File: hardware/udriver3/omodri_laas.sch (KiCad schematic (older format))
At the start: 0 parts

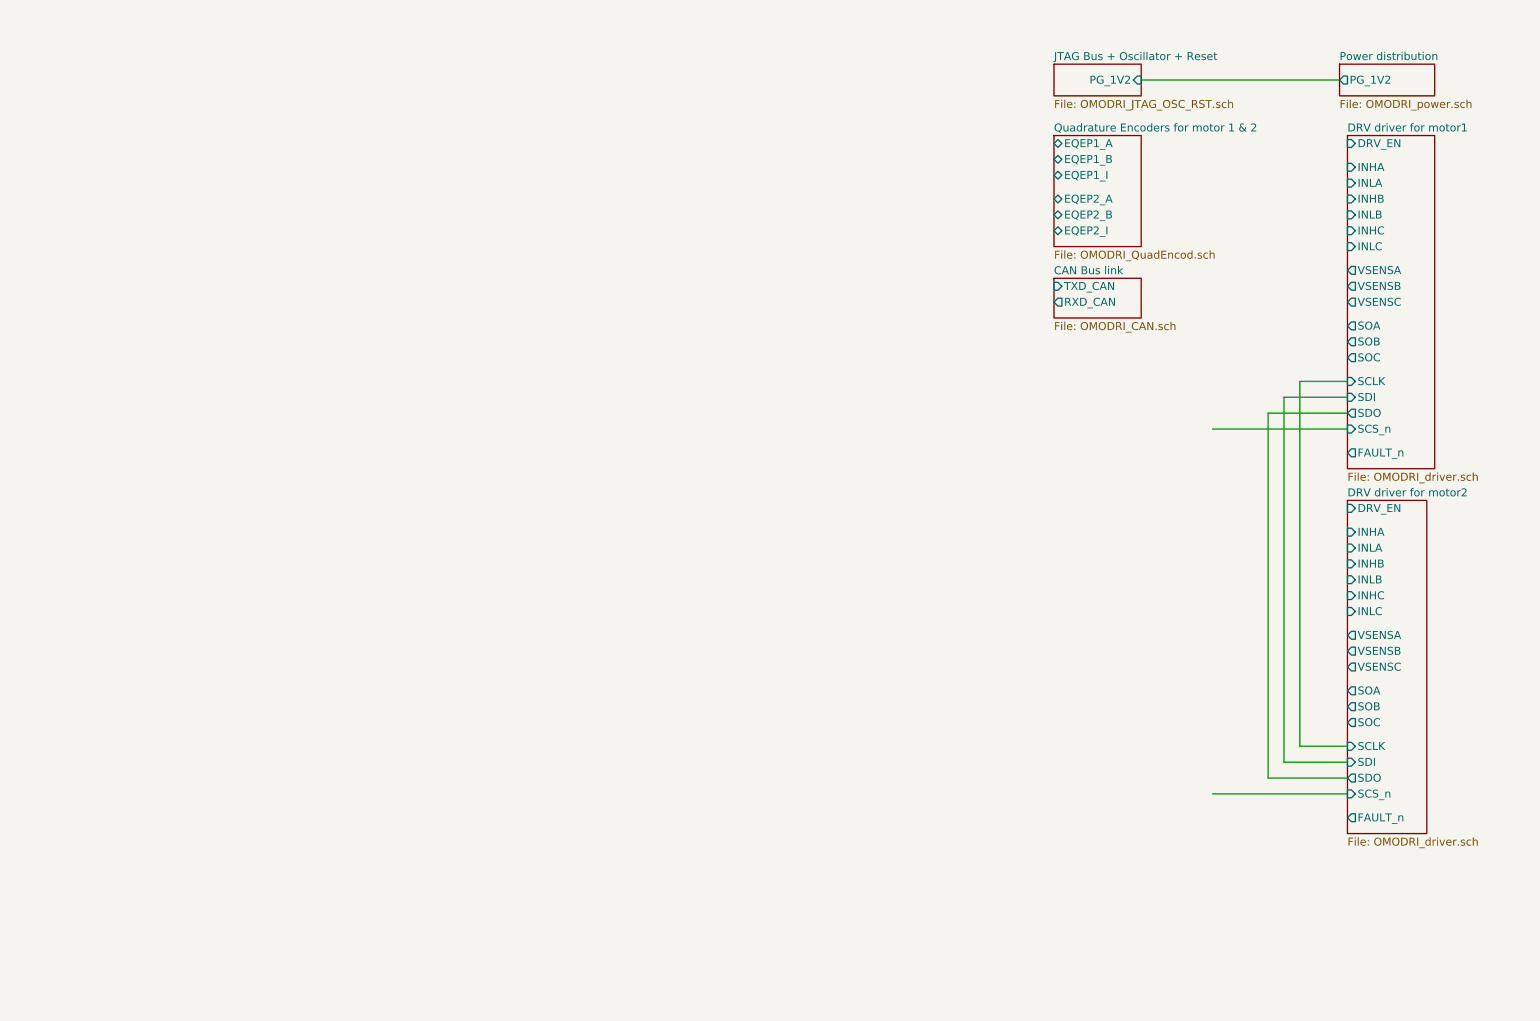
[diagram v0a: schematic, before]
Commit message: Update of the BOM. Not yet finished.
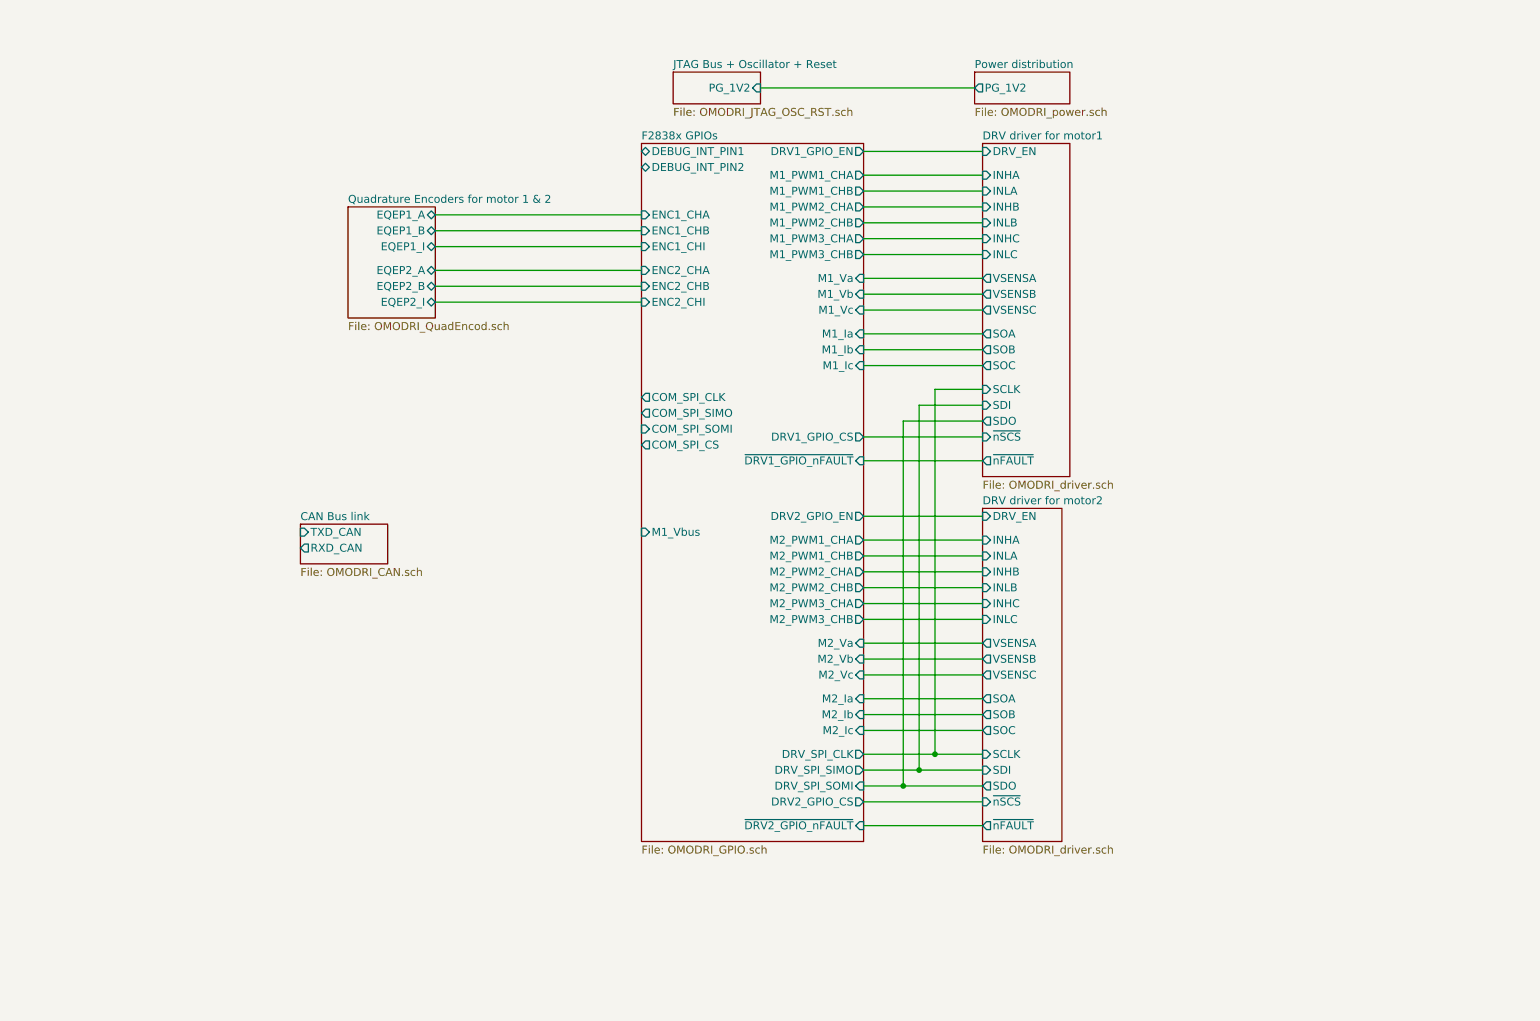
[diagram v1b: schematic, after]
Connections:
- wire segments 12 -> 49

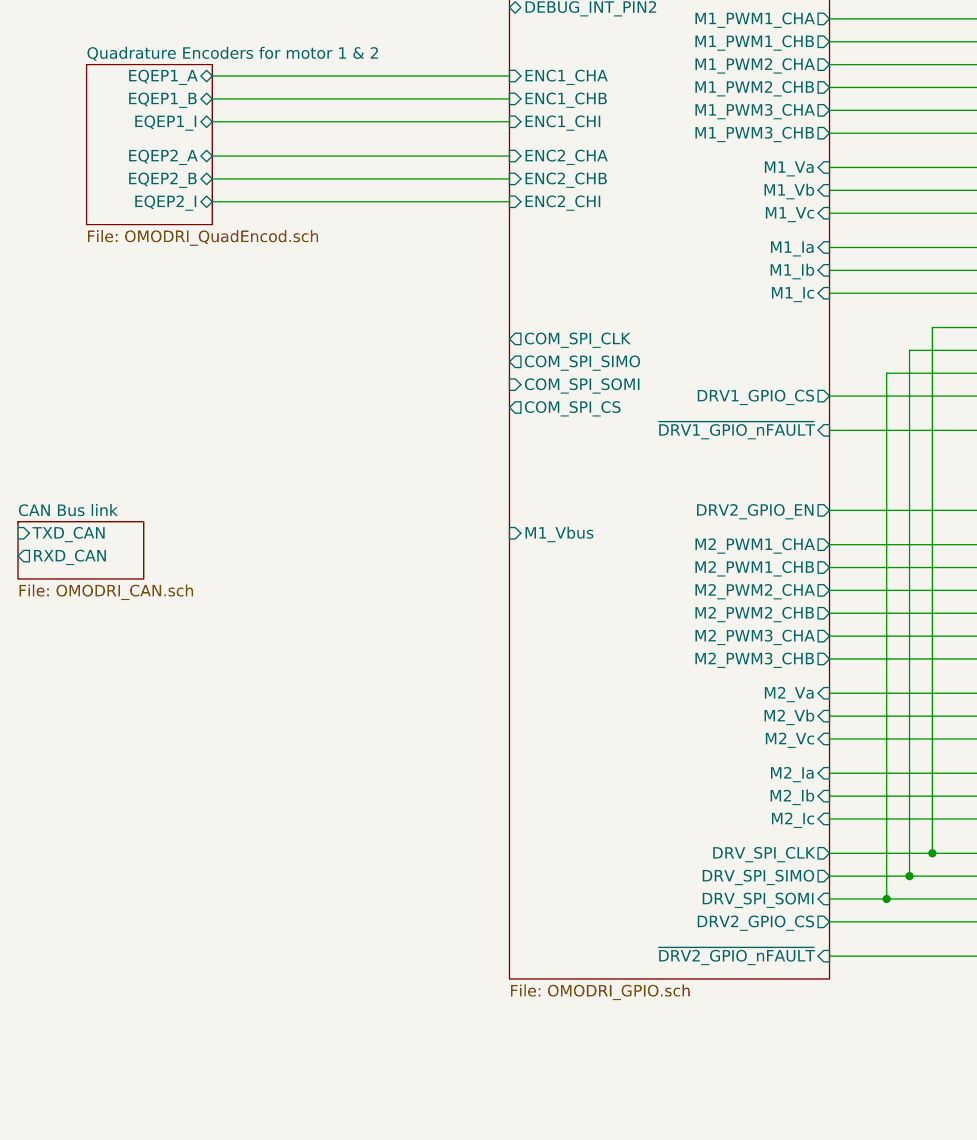
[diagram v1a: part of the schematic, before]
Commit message: Updated version with 28388D pin matching PAL design.
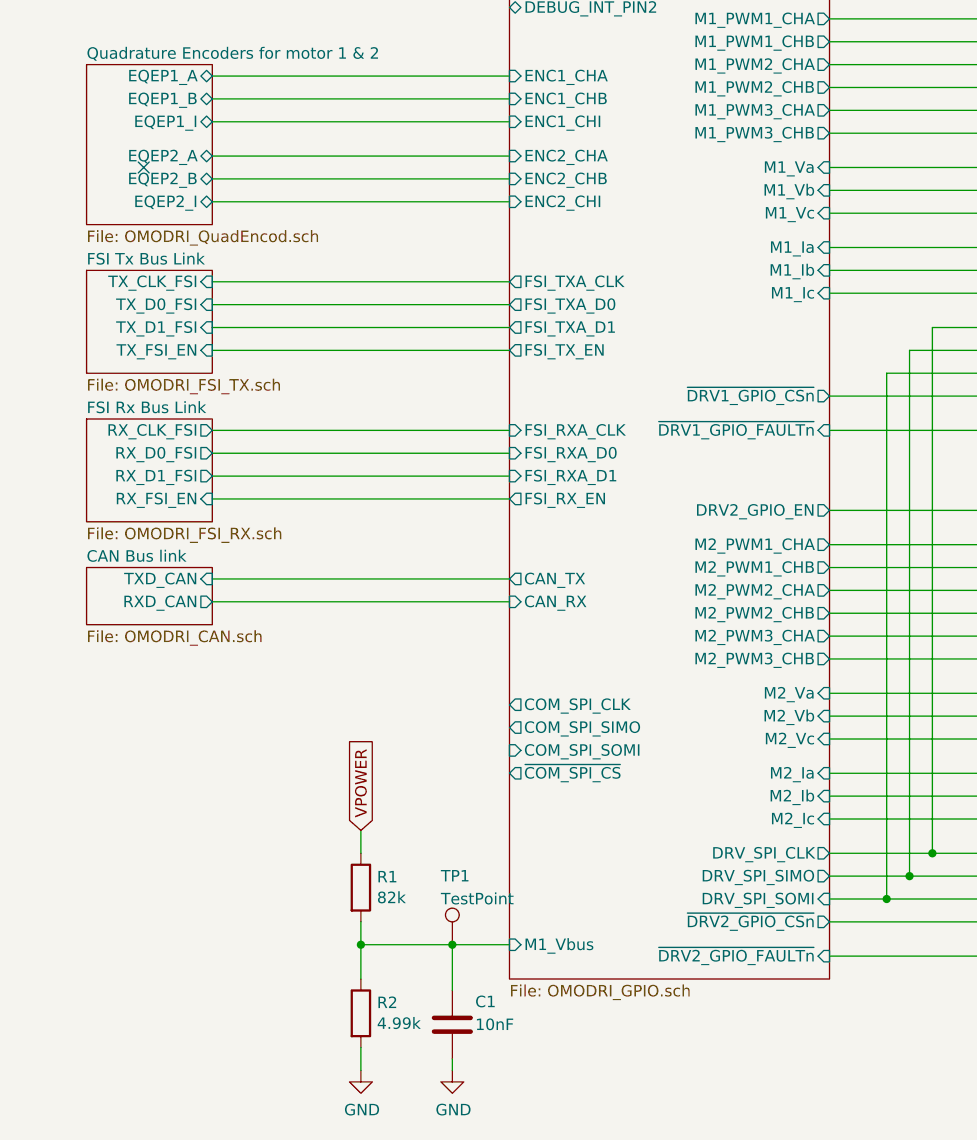
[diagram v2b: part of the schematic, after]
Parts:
- added C1: 10nF, Capacitor_SMD:C_0201_0603Metric, symbol Device:C
- added R1: 82k, Resistor_SMD:R_0603_1608Metric, symbol Device:R
- added R2: 4.99k, Resistor_SMD:R_0603_1608Metric, symbol Device:R
- added TP1: TestPoint, TestPoint:TestPoint_Pad_D1.5mm, symbol Connector:TestPoint
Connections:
- net F2838x GPIOs/M1_Vbus: now also C1.1, R1.2, R2.1, TP1.1
- new net GND: C1.2, R2.2
- new net VPOWER: R1.1
- no-connect marks 0 -> 1

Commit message: All footprints are present. DRV with 2 power branches.
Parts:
- added C10, C2, C9: 10nF, Capacitor_SMD:C_0201_0603Metric, symbol Device:C
- added C3, C4, C5, C6, C7, C8: 100uF, Capacitor_Tantalum_SMD:CP_EIA-7360-38_Kemet-E, symbol Device:CP
- added D1: WS2812B, LED_SMD:LED_WS2812B_PLCC4_5.0x5.0mm_P3.2mm, symbol LED:WS2812B
- added J1: Conn_01x12, Connector_Hirose:Hirose_DF13-12P-1.25DSA_1x12_P1.25mm_Vertical, symbol Connector_Generic:Conn_01x12
- added J2: Conn_01x05, Connector_Hirose:Hirose_DF13-05P-1.25DSA_1x05_P1.25mm_Vertical, symbol Connector_Generic:Conn_01x05
- added J3, J5: Conn_01x03, Connector_Hirose:Hirose_DF13-03P-1.25DSA_1x03_P1.25mm_Vertical, symbol Connector_Generic:Conn_01x03
- added J4: Conn_01x02, Connector_AMASS:AMASS_XT30PW-M_1x02_P2.50mm_Horizontal, symbol Connector_Generic:Conn_01x02
- added R3: 120, Resistor_SMD:R_0201_0603Metric, symbol Device:R
- added R4: 5.1k, Resistor_SMD:R_0402_1005Metric, symbol Device:R
- added TP2: TestPoint, TestPoint:TestPoint_Pad_D1.0mm, symbol Connector:TestPoint
- C1: value 10nF -> 100nF; DigiKey 490-14454-1-ND -> 490-14450-1-ND; Farnell 2990696 -> 2990681; Mouser 81-GRM033R71E103KE4D -> 81-GRM033C71A104KE4D; Part No GRM033R71E103KE14D -> GRM033C71A104KE14D; RS 185-2059 -> 185-1751; Rated Voltage 25V -> 10V
- R1: value 82k -> 120; footprint Resistor_SMD:R_0603_1608Metric -> Resistor_SMD:R_0201_0603Metric; DigiKey (none) -> P122692CT-ND; Farnell (none) -> 2396857; Mouser (none) -> 667-ERJ-1GNF1200C; Part No (none) -> ERJ-1GNF1200C
- R2: value 4.99k -> 100k; footprint Resistor_SMD:R_0603_1608Metric -> Resistor_SMD:R_0402_1005Metric; DigiKey (none) -> P100KLCT-ND; Farnell (none) -> 2302839; Mouser (none) -> 667-ERJ-2RKF1003X; Part No (none) -> ERJ-2RKF1003X; RS (none) -> 732-5255; Rated Voltage (none) -> 50
- TP1: footprint TestPoint:TestPoint_Pad_D1.5mm -> TestPoint:TestPoint_Pad_D1.0mm
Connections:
- net labels added: GNDA, VDDA_3V3, VDD_3V3
- wire segments 67 -> 117

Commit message: First complete release. No EtherCAT, IO ready to be connected.
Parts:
- removed J1: Conn_01x12, Connector_Hirose:Hirose_DF13-12P-1.25DSA_1x12_P1.25mm_Vertical, symbol Connector_Generic:Conn_01x12
- removed R3: 120, Resistor_SMD:R_0201_0603Metric, symbol Device:R
- added J1: Conn_01x11, Connector_Hirose:Hirose_DF13-11P-1.25DSA_1x11_P1.25mm_Vertical, symbol Connector_Generic:Conn_01x11
- added R4: 120, Resistor_SMD:R_0201_0603Metric, symbol Device:R
- added TP1, TP2, TP3, TP4: TestPoint, TestPoint:TestPoint_Pad_D1.0mm, symbol Connector:TestPoint
- renumbered C3 to C2, C4 to C3, C5 to C4, C2 to C5, R2 to R1, R1 to R2, R4 to R3, TP1 to TP5, TP2 to TP6
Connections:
- wire segments 117 -> 130
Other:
- moved on the sheet: C1, C2, C3, C4, C5, C6, C7, C8, C9, D1, J3, J4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

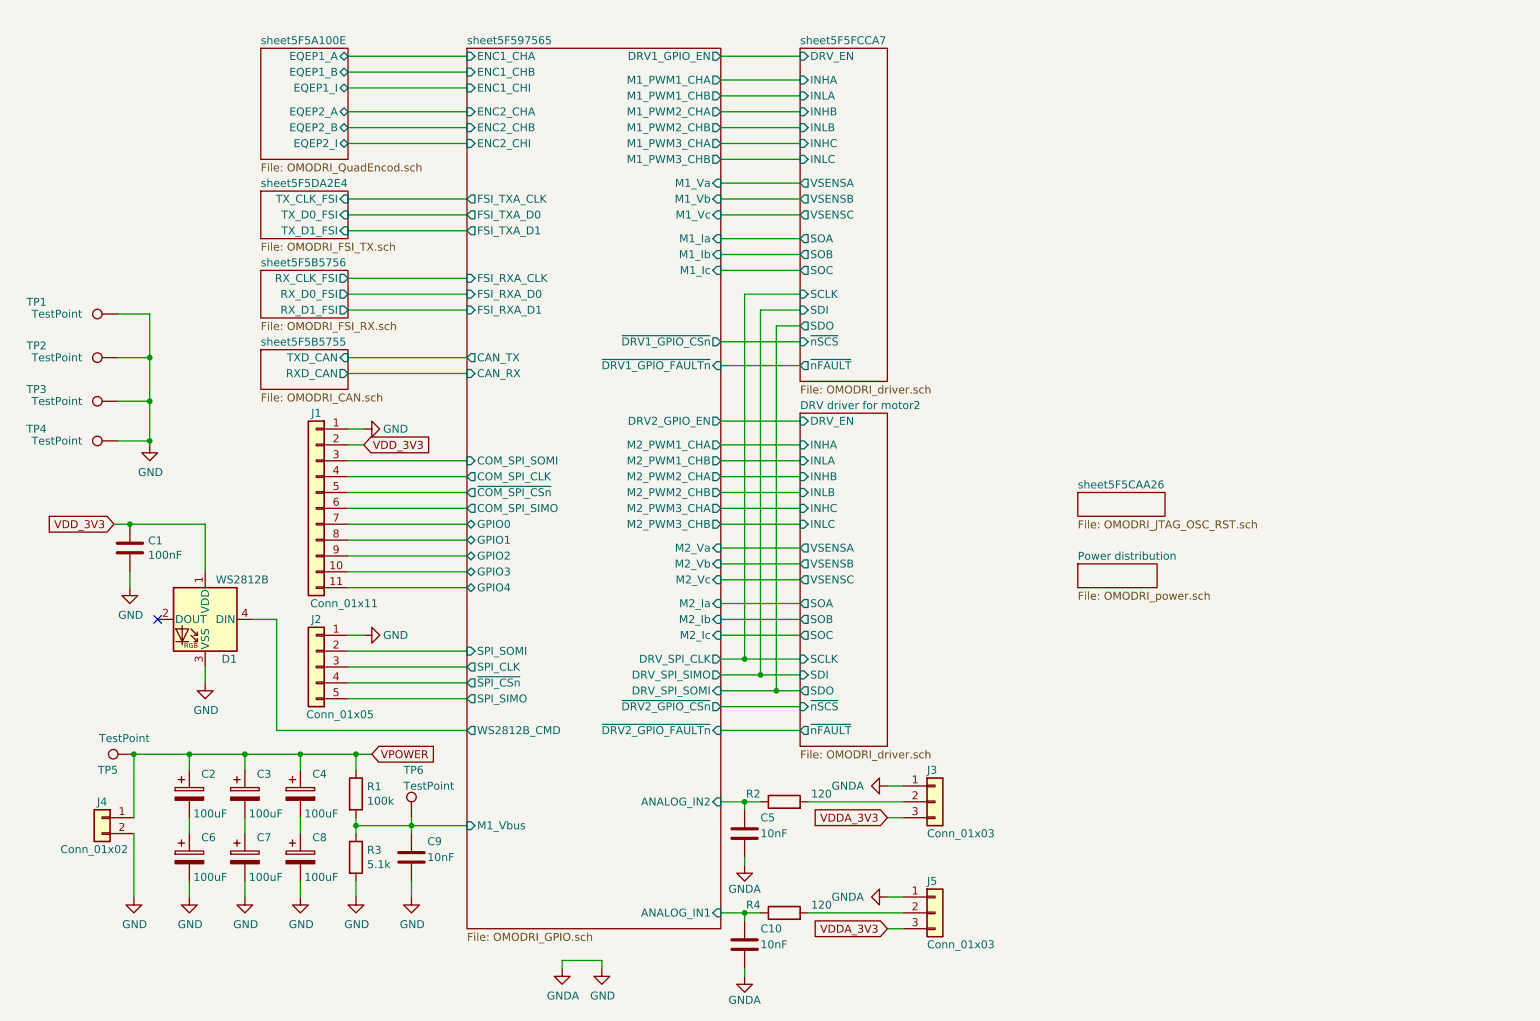
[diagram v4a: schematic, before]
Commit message: Update of the schematics. Driver and power files split. Placement starting.
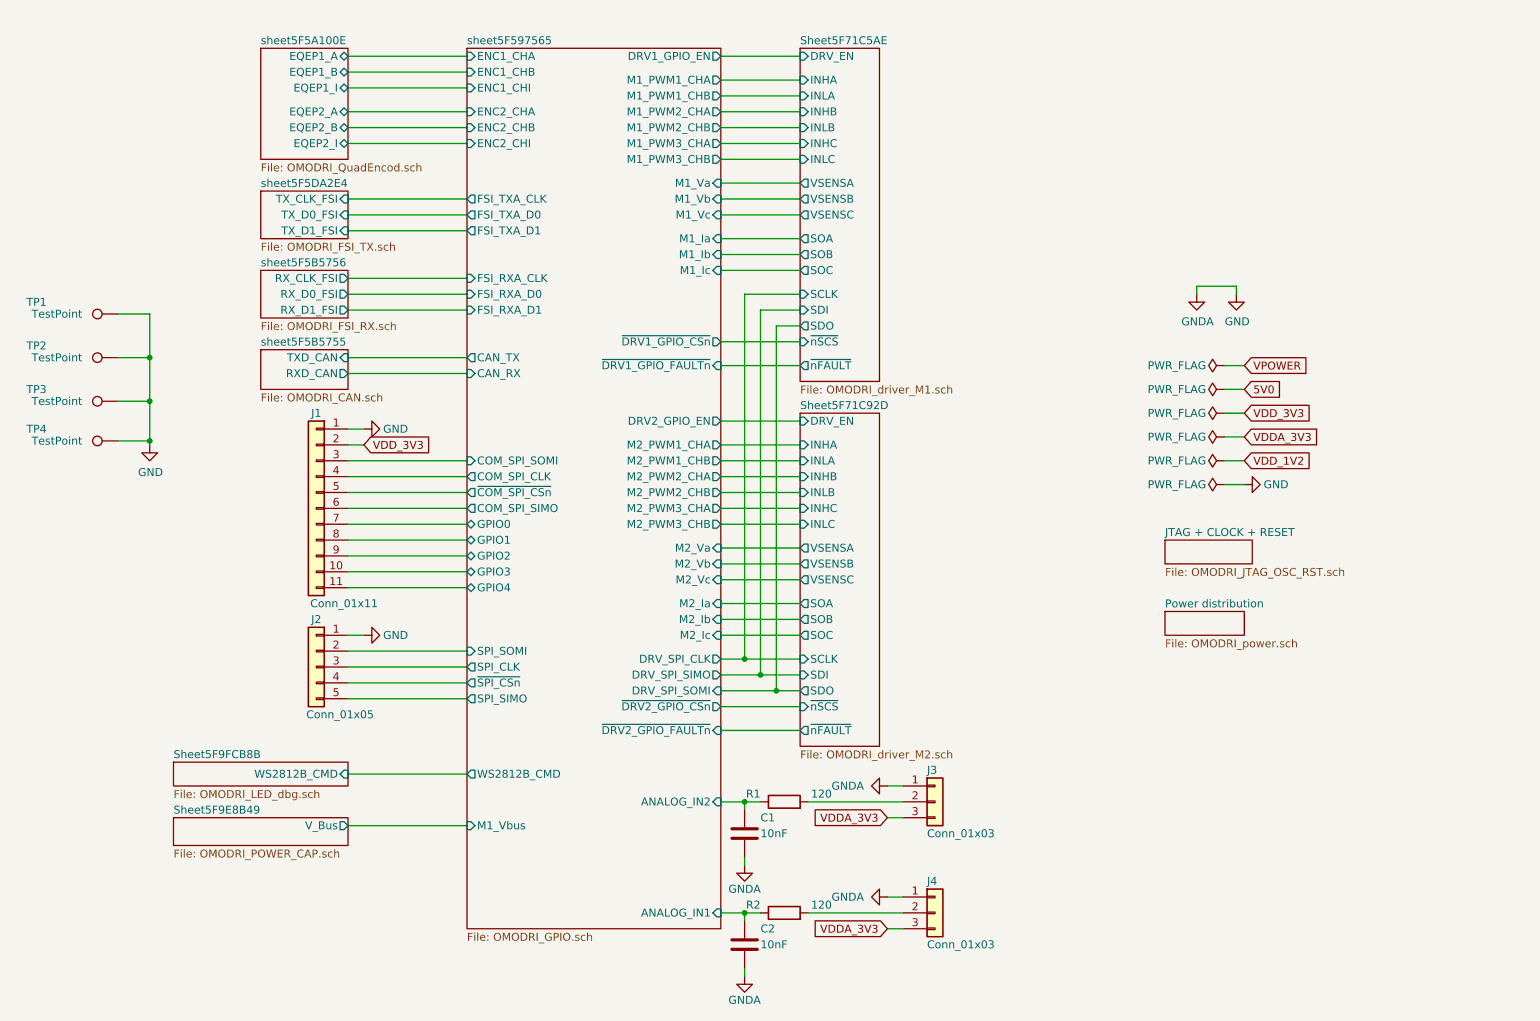
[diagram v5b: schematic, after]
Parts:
- removed C1: 100nF, Capacitor_SMD:C_0201_0603Metric, symbol Device:C
- removed C2, C3, C4, C6, C7, C8: 100uF, Capacitor_Tantalum_SMD:CP_EIA-7360-38_Kemet-E, symbol Device:CP
- removed C9: 10nF, Capacitor_SMD:C_0201_0603Metric, symbol Device:C
- removed D1: WS2812B, LED_SMD:LED_WS2812B_PLCC4_5.0x5.0mm_P3.2mm, symbol LED:WS2812B
- removed J4: Conn_01x02, Connector_AMASS:AMASS_XT30PW-M_1x02_P2.50mm_Horizontal, symbol Connector_Generic:Conn_01x02
- removed R1: 100k, Resistor_SMD:R_0402_1005Metric, symbol Device:R
- removed R3: 5.1k, Resistor_SMD:R_0402_1005Metric, symbol Device:R
- removed TP5, TP6: TestPoint, TestPoint:TestPoint_Pad_D1.0mm, symbol Connector:TestPoint
- J1: DigiKey (none) -> H126373-ND; Mouser (none) -> 798-DF13-11P125DSA75; Part No (none) -> DF13-11P-1.25DSA(75); RS (none) -> 188-6390
- J2: DigiKey (none) -> DF13-5P-1.25DSA(75)-ND; Farnell (none) -> 2427589; Mouser (none) -> 798-DF13-5P-125DSA75; Part No (none) -> DF13-5P-1.25DSA(75); RS (none) -> 188-6358
- J3: DigiKey (none) -> DF13-3P-1.25DSA(75)-ND; Farnell (none) -> 2916340; Mouser (none) -> 798-DF13-3P-125DSA75; Part No (none) -> DF13-3P-1.25DSA(75); RS (none) -> 188-6281
- J4: renamed from J5; DigiKey (none) -> DF13-3P-1.25DSA(75)-ND; Farnell (none) -> 2916340; Mouser (none) -> 798-DF13-3P-125DSA75; Part No (none) -> DF13-3P-1.25DSA(75); RS (none) -> 188-6281
- renumbered C5 to C1, C10 to C2, R2 to R1, R4 to R2
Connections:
- no-connect marks 1 -> 0
